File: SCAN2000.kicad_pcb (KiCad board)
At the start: 2 copper layers, 228.6 x 70.6 mm, 132 parts, among them J1 Conn_02x16_Row_Letter_First, J2 Conn_01x05, J3 Conn_01x02, J4 Screw_Terminal_01x02, J5 Screw_Terminal_01x10, J6 Screw_Terminal_01x10, J7 Screw_Terminal_01x02, J8 Screw_Terminal_01x10, J9 Screw_Terminal_01x10, U1 TPS73233DBVR, U10 TLP3558A, U11 TLP3558A, U12 TLP3558A, U13 TLP3558A, U14 TLP3558A, U15 TLP3558A, U16 TLP3558A, U17 TLP3558A, U18 TLP3558A, U19 TLP3558A, U20 TLP3558A, U21 TLP3558A, U22 TLP3558A, U23 TLP3558A, U24 TLP3558A, U25 TLP3558A, U26 TLP3558A, U27 TLP3558A, U28 TLP3558A, U29 TLP3558A, U3 STM32G070KBT6, U30 TLP3558A, U31 TLP3558A, U32 TLP3558A, U33 TLP3558A, U34 TLP3558A, U35 TLP3558A, U36 TLP3558A, U37 TLP3558A, U38 TLP3558A, U39 TLP3558A, U4 TLP3558A, U40 TLP3558A, U41 TLP3558A, U42 TLP3558A, U43 TLP3558A, U44 TLP3558A, U45 TLP3558A, U46 TLP3558A, U47 TLP3558A, U5 TLP3558A, U6 TLP3558A, U7 TLP3558A, U8 TLP3558A, U9 TLP3558A

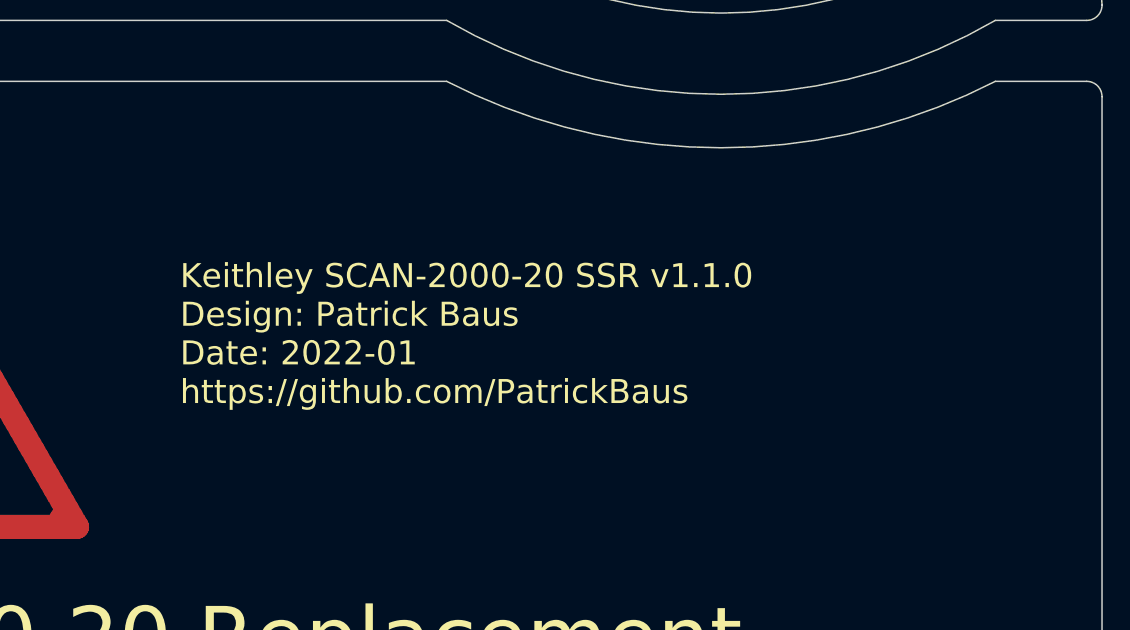
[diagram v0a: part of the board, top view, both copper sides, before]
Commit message: Add CI script (#2)
* Renamed main files to SCAN2000

* Add CI

* Bump version to 1.1.1

* Remove the BOM as this is now generated content

* Reworked Readme
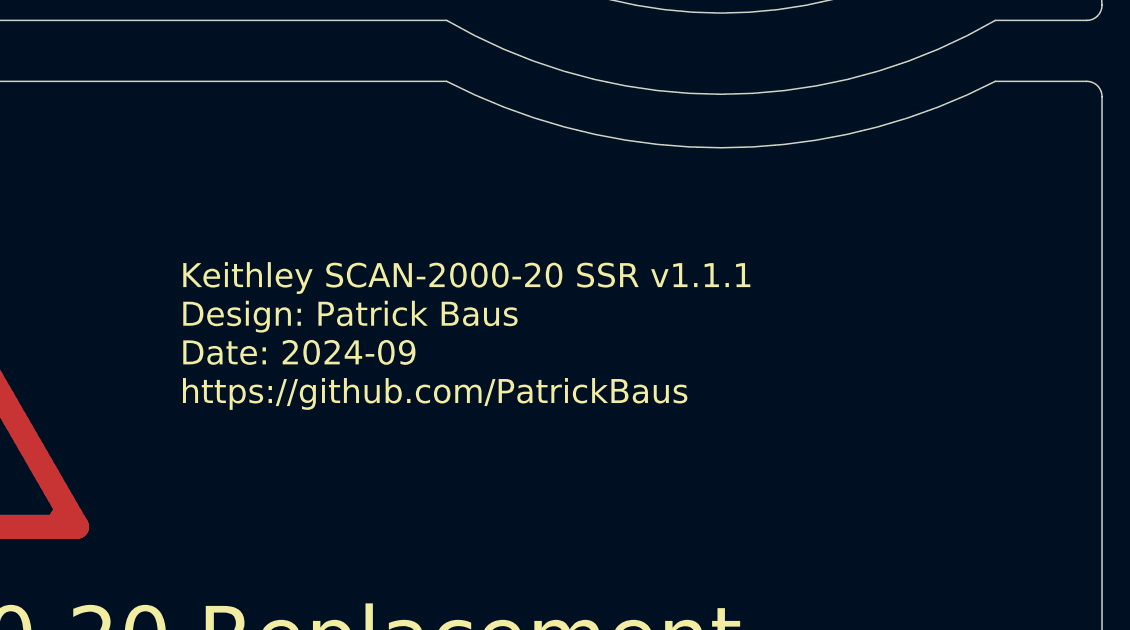
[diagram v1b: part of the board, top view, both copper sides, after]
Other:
- board text added: "Keithley SCAN-2000-20 SSR v1.1.1 Design: Patrick Baus Date: 2024-09 https://github.com/PatrickBaus"
- board text removed: "Keithley SCAN-2000-20 SSR v1.1.0 Design: Patrick Baus Date: 2022-01 https://github.com/PatrickBaus"
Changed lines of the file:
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@@
 		)
 		(sheetname "Root")
-		(sheetfile "main.kicad_sch")
+		(sheetfile "SCAN2000.kicad_sch")
 		(attr exclude_from_pos_files exclude_from_bom allow_missing_courtyard)
 		(fp_line
@@
 		(property ki_fp_filters "R_*")
 		(sheetname "Root")
-		(sheetfile "main.kicad_sch")
+		(sheetfile "SCAN2000.kicad_sch")
 		(attr smd)
 		(fp_line
@@
 		(property ki_fp_filters "Pin* Test*")
 		(sheetname "Root")
-		(sheetfile "main.kicad_sch")
+		(sheetfile "SCAN2000.kicad_sch")
 		(attr through_hole dnp)
 		(fp_circle
@@
 		(property ki_fp_filters "SolderJumper*Bridged12*")
 		(sheetname "Root")
-		(sheetfile "main.kicad_sch")
+		(sheetfile "SCAN2000.kicad_sch")
 		(zone_connect 1)
 		(attr exclude_from_pos_files exclude_from_bom)
@@
 			)
 		)
-		(property "MFN" "Nichicon"
+		(property "MFN" "Rubycon"
 			(at -50.292 132.588 0)
 			(layer "F.Fab")
@@
 			)
 		)
-		(property "PN" "ULD2A100MED1TD"
+		(property "PN" "100YXM10MEFR6"
 			(at -50.292 132.588 0)
 			(layer "F.Fab")
@@
 			)
 		)
-		(property "Temperature" "Tstorage = –25 °C to 105 °C"
+		(property "Temperature" "Tstorage = –40 °C to 105 °C"
 			(at 0 0 -90)
 			(unlocked yes)
@@
 		(property ki_fp_filters "CP_*")
 		(sheetname "Root")
-		(sheetfile "main.kicad_sch")
+		(sheetfile "SCAN2000.kicad_sch")
 		(attr through_hole)
 		(fp_line
@@
 		(property ki_fp_filters "Pin* Test*")
 		(sheetname "Root")
-		(sheetfile "main.kicad_sch")
+		(sheetfile "SCAN2000.kicad_sch")
 		(attr through_hole dnp)
 		(fp_circle
@@
 		)
 		(sheetname "Root")
-		(sheetfile "main.kicad_sch")
+		(sheetfile "SCAN2000.kicad_sch")
 		(attr exclude_from_pos_files exclude_from_bom)
 		(fp_poly
@@
 		(property ki_fp_filters "R_*")
 		(sheetname "Root")
-		(sheetfile "main.kicad_sch")
+		(sheetfile "SCAN2000.kicad_sch")
 		(attr smd)
 		(fp_line
@@
 		(property ki_fp_filters "R_*")
 		(sheetname "Root")
-		(sheetfile "main.kicad_sch")
+		(sheetfile "SCAN2000.kicad_sch")
 		(attr smd)
 		(fp_line
@@
 		(property ki_fp_filters "R_*")
 		(sheetname "Root")
-		(sheetfile "main.kicad_sch")
+		(sheetfile "SCAN2000.kicad_sch")
 		(attr smd)
 		(fp_line
@@
 		(property ki_fp_filters "Connector*:*_2x??_*")
 		(sheetname "Root")
-		(sheetfile "main.kicad_sch")
+		(sheetfile "SCAN2000.kicad_sch")
 		(attr through_hole)
 		(fp_line
@@
 		(property ki_fp_filters "Pin* Test*")
 		(sheetname "Root")
-		(sheetfile "main.kicad_sch")
+		(sheetfile "SCAN2000.kicad_sch")
 		(attr through_hole)
 		(fp_circle
@@
 		(property ki_fp_filters "R_*")
 		(sheetname "Root")
-		(sheetfile "main.kicad_sch")
+		(sheetfile "SCAN2000.kicad_sch")
 		(attr smd)
 		(fp_line
@@
 		(property ki_fp_filters "R_*")
 		(sheetname "Root")
-		(sheetfile "main.kicad_sch")
+		(sheetfile "SCAN2000.kicad_sch")
 		(attr smd)
 		(fp_line
@@
 		(property ki_fp_filters "Pin* Test*")
 		(sheetname "Root")
-		(sheetfile "main.kicad_sch")
+		(sheetfile "SCAN2000.kicad_sch")
 		(attr through_hole dnp)
 		(fp_circle
@@
 		(layer "Edge.Cuts")
 	)
-	(gr_text "Keithley SCAN-2000-20 SSR v1.1.0\nDesign: Patrick Baus\nDate: 2022-01\nhttps://github.com/PatrickBaus"
+	(gr_text "Keithley SCAN-2000-20 SSR v1.1.1\nDesign: Patrick Baus\nDate: 2024-09\nhttps://github.com/PatrickBaus"
 		(at 223.266 61.76 0)
 		(layer "F.SilkS")
